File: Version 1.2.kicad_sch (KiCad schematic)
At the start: 33 parts, among them J1 Conn_01x04_Pin, J2 Screw_Terminal_01x02, J3 Conn_01x07_Pin, J4 Conn_Coaxial, U1 BGA2801, U2 BGA420, U3 AS179-92LF, U4 SX1278, U5 74LVC1G19, Y1 ECS-TXO-2520-33-400-AN-TR

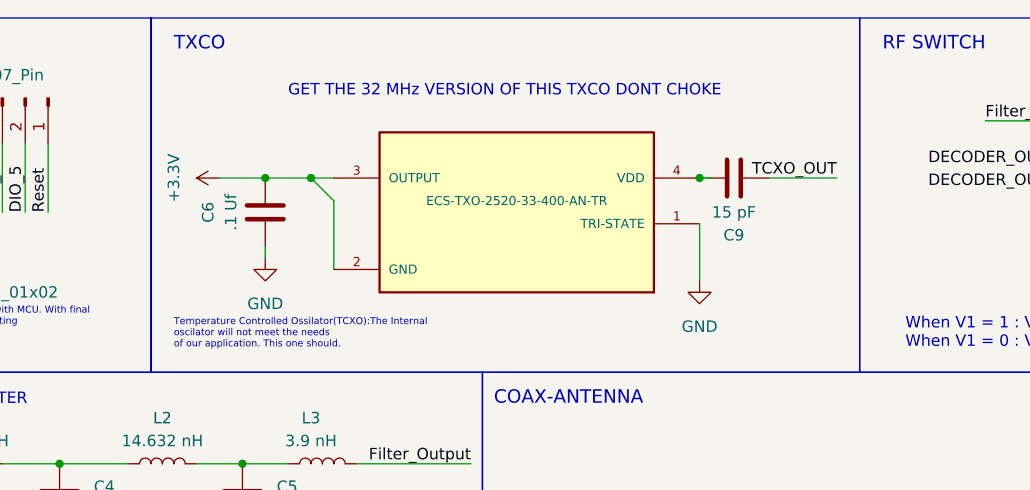
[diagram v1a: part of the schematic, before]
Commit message: Fix Clock Pads
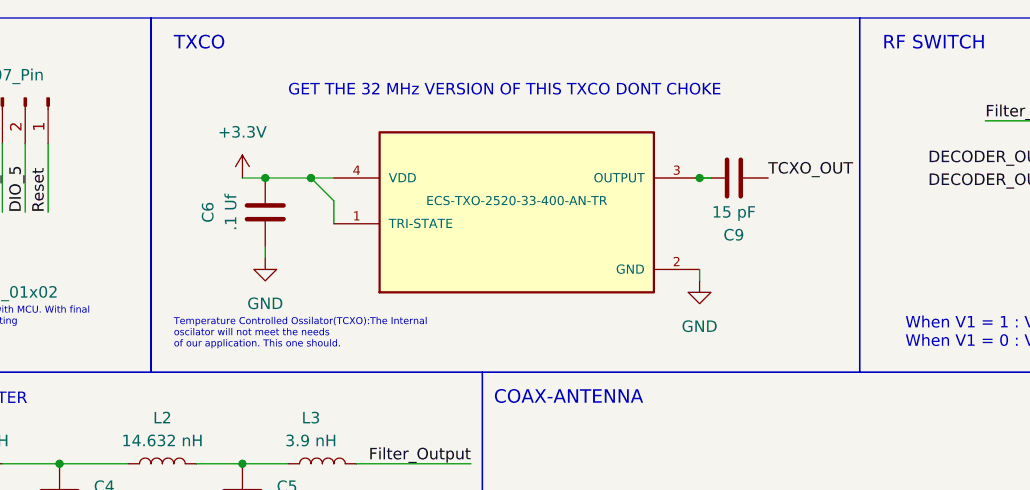
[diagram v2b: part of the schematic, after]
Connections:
- net +3.3V: now also Y1.1 (TRI-STATE), Y1.4 (VDD); no longer Y1.2 (GND), Y1.3 (OUTPUT)
- net GND: now also Y1.2 (GND); no longer Y1.1 (TRI-STATE)
- net at C9.1: now also Y1.3 (OUTPUT); no longer Y1.4 (VDD)
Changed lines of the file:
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@@
     (stroke (width 0) (type default))
   )
-  (wire (pts (xy 80.01 35.56) (xy 80.01 43.18))
+  (wire (pts (xy 80.01 35.56) (xy 80.01 38.1))
     (stroke (width 0) (type default))
   )
@@
     (stroke (width 0) (type default))
   )
-  (wire (pts (xy 67.31 33.02) (xy 72.39 33.02))
+  (wire (pts (xy 69.85 33.02) (xy 72.39 33.02))
     (stroke (width 0) (type default))
   )
@@
     (stroke (width 0) (type default))
   )
+  (wire (pts (xy 120.65 43.18) (xy 120.65 44.45))
+    (stroke (width 0) (type default))
+  )
   (wire (pts (xy 198.12 114.3) (xy 214.63 114.3))
     (stroke (width 0) (type default))
@@
     (stroke (width 0) (type default))
   )
-  (wire (pts (xy 120.65 38.1) (xy 120.65 44.45))
-    (stroke (width 0) (type default))
-  )
   (wire (pts (xy 214.63 127) (xy 207.01 127))
     (stroke (width 0) (type default))
@@
   )
   (wire (pts (xy 143.51 121.92) (xy 149.86 121.92))
-    (stroke (width 0) (type default))
-  )
-  (wire (pts (xy 128.27 33.02) (xy 135.89 33.02))
     (stroke (width 0) (type default))
   )
@@
     (effects (font (size 1.27 1.27)) (justify left bottom))
   )
+  (label "TCXO_OUT" (at 128.27 33.02 0) (fields_autoplaced)
+    (effects (font (size 1.27 1.27)) (justify left bottom))
+  )
   (label "MISO" (at 201.93 139.7 0) (fields_autoplaced)
     (effects (font (size 1.27 1.27)) (justify left bottom))
@@
   (label "PA_OUTPUT" (at 82.55 121.92 0) (fields_autoplaced)
     (effects (font (size 1.27 1.27)) (justify left bottom))
-  )
-  (label "TCXO_OUT" (at 135.89 33.02 180) (fields_autoplaced)
-    (effects (font (size 1.27 1.27)) (justify right bottom))
   )
   (label "DIO_1" (at 207.01 121.92 0) (fields_autoplaced)
@@
     )
   )
-  (symbol (lib_id "TXCO #2:ECS-TXO-2520-33-400-AN-TR") (at 100.33 35.56 0) (mirror y) (unit 1)
+  (symbol (lib_id "TXCO #2:ECS-TXO-2520-33-400-AN-TR") (at 100.33 35.56 0) (unit 1)
     (in_bom yes) (on_board yes) (dnp no)
-    (property "Reference" "Y1" (at 101.6 34.29 0)
+    (property "Reference" "Y1" (at 99.06 34.29 0)
       (effects (font (size 1.27 1.27)) hide)
     )
@@
     )
   )
+  (symbol (lib_id "power:+3.3V") (at 69.85 33.02 0) (unit 1)
+    (in_bom yes) (on_board yes) (dnp no) (fields_autoplaced)
+    (property "Reference" "#PWR033" (at 69.85 36.83 0)
+      (effects (font (size 1.27 1.27)) hide)
+    )
+    (property "Value" "+3.3V" (at 69.85 27.94 0)
+      (effects (font (size 1.27 1.27)))
+    )
+    (property "Footprint" "" (at 69.85 33.02 0)
+      (effects (font (size 1.27 1.27)) hide)
+    )
+    (property "Datasheet" "" (at 69.85 33.02 0)
+      (effects (font (size 1.27 1.27)) hide)
+    )
+    (pin "1")
+    (instances
+      (project "Version 1.2"
+        (path "/68ad03eb-4fd6-4077-892a-018e34de02c8"
+          (reference "#PWR033") (unit 1)
+        )
+      )
+    )
+  )
   (symbol (lib_id "74xGxx:74LVC1G19") (at 246.38 35.56 0) (unit 1)
     (in_bom yes) (on_board yes) (dnp no)
@@
         )
       )
-    )
-  )
-  (symbol (lib_id "power:+3.3V") (at 67.31 33.02 90) (unit 1)
-    (in_bom yes) (on_board yes) (dnp no)
-    (property "Reference" "#PWR08" (at 71.12 33.02 0)
-      (effects (font (size 1.27 1.27)) hide)
-    )
-    (property "Value" "+3.3V" (at 62.23 33.02 0)
-      (effects (font (size 1.27 1.27)))
-    )
-    (property "Footprint" "" (at 67.31 33.02 0)
-      (effects (font (size 1.27 1.27)) hide)
-    )
-    (property "Datasheet" "" (at 67.31 33.02 0)
-      (effects (font (size 1.27 1.27)) hide)
-    )
-    (pin "1")
-    (instances
-      (project "Version 1.2"
-        (path "/68ad03eb-4fd6-4077-892a-018e34de02c8"
-          (reference "#PWR08") (unit 1)
-        )
-      )
-      (project "Version1.0"
-        (path "/a5904a20-3abc-4571-9db8-deadedb7a006"
-          (reference "#PWR010") (unit 1)
-        )
-      )
